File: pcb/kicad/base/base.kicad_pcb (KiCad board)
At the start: 2 copper layers, 94 parts, among them J1 CHIP_EN, J2 Vbatt_I-test, P1 J-Link SWD, P2 SMA, P3 Power Source, P4 CONN_01X08, U1 SAMB11G18A-edit, U2 XBee-PRO_900HP, Y1 32.768kHz, Y2 26MHz

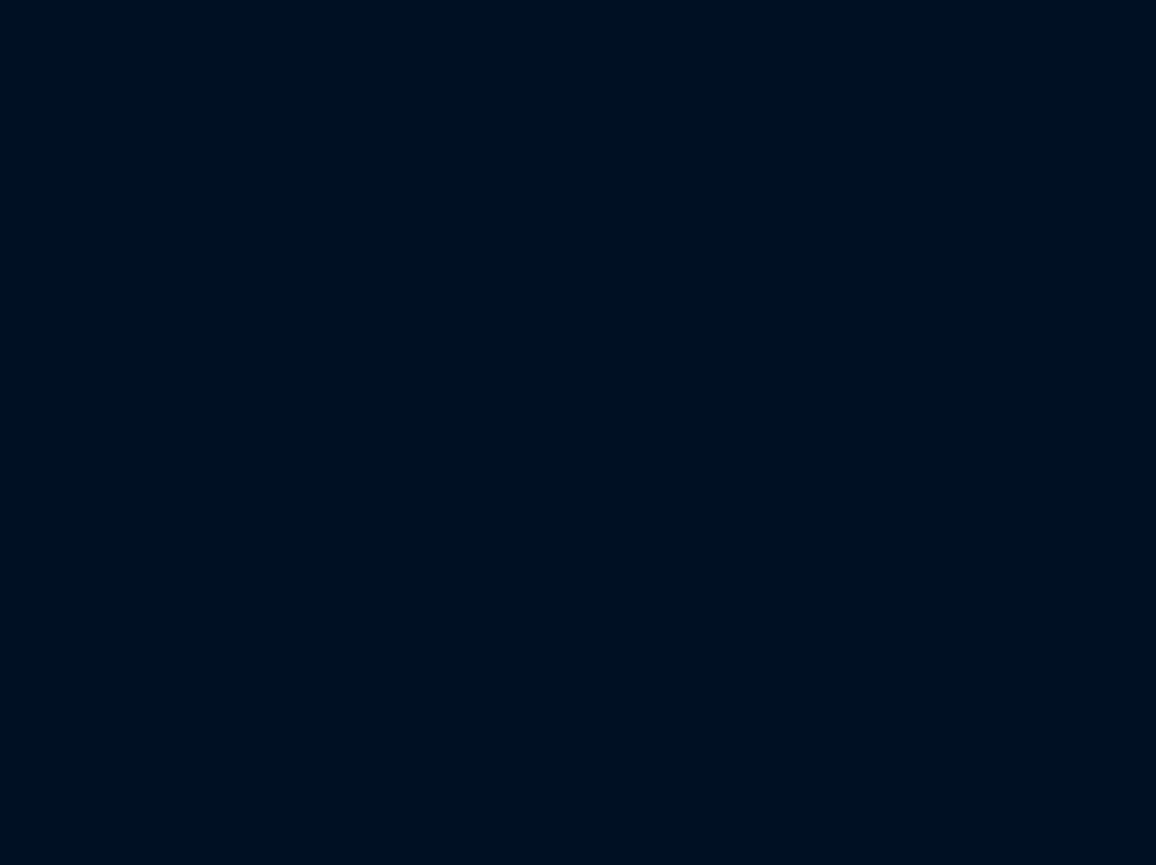
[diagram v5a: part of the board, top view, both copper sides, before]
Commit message: Add 16x4 LCD display symbol
Symbol and schematic started for the Crystalfontz display to be used
for user interface. Display contrast and LCD brightness settings need
to configured based on breadboard testing. Layout will be reworked to
properly accompany the mass pin usage of the display.
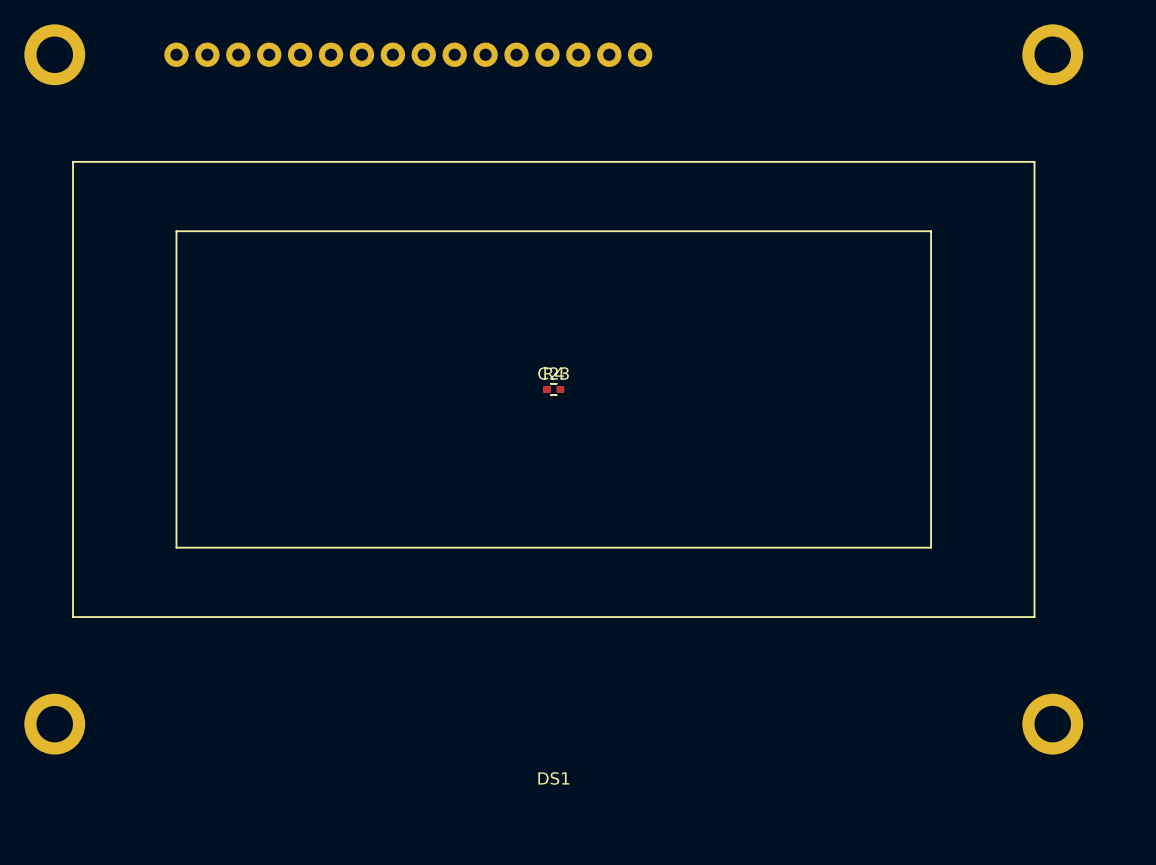
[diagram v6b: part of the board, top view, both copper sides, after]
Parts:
- added C23: C_Small, Capacitors_SMD:C_0402, F.Cu at (0.00, 0.00)
- added DS1: LCD16X4, CFAH1604A, F.Cu at (0.00, 0.00)
- added R4: 100, Capacitors_SMD:C_0402, F.Cu at (0.00, 0.00)
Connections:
- U1 pad 10: Net-(U1-Pad10) -> /DISP_B4
- U1 pad 11: Net-(U1-Pad11) -> /DISP_B3
- U1 pad 12: Net-(U1-Pad12) -> /DISP_B2
- U1 pad 13: /LP_GPIO_6 -> /DISP_B1
- U1 pad 14: /LP_GPIO_7 -> /DISP_B0
- U1 pad 15: /LP_GPIO_8 -> /DISP_E
- U1 pad 16: /LP_GPIO_9 -> /DISP_RW
- U1 pad 17: /LP_GPIO_10 -> /DISP_REG
- U1 pad 18: /LP_GPIO_11 -> Net-(U1-Pad18)
- U1 pad 19: /LP_GPIO_12 -> Net-(U1-Pad19)
- U1 pad 20: /LP_GPIO_13 -> Net-(U1-Pad20)
- U1 pad 7: Net-(U1-Pad7) -> /DISP_B7
- U1 pad 8: Net-(U1-Pad8) -> /DISP_B6
- U1 pad 9: Net-(U1-Pad9) -> /DISP_B5
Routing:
- net /LP_GPIO_6: track 33.6 -> 29.5 mm
- net /DISP_B1: track 0.00 -> 4.13 mm
- net /DISP_B0: track 0.00 -> 3.96 mm
- net /LP_GPIO_7: track 35.7 -> 31.7 mm
- net /LP_GPIO_8: track 37.7 -> 33.9 mm
- net /DISP_E: track 0.00 -> 3.79 mm
- net /LP_GPIO_9: track 39.8 -> 36.1 mm
- net /DISP_RW: track 0.00 -> 3.62 mm
- net /LP_GPIO_10: track 41.8 -> 38.3 mm
- net /DISP_REG: track 0.00 -> 3.45 mm
- net Net-(U1-Pad18): track 0.00 -> 3.28 mm
- net /LP_GPIO_11: track 43.8 -> 40.6 mm
- net Net-(U1-Pad19): track 0.00 -> 3.11 mm
- net /LP_GPIO_12: track 45.9 -> 42.8 mm
- net Net-(U1-Pad20): track 0.00 -> 2.93 mm
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
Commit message: Cleanup previous revision traces for new layout
Moving forward with full base station layout. Crystals, power caps, and
2.4GHz antenna placed. Mounting hole placements should coincide with
display mounting holes. May want to rotate XBee placement to allow push
buttons to be placed to the right of the display.
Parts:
- removed J1: CHIP_EN, Misc:Socket_Strip_Straight_1x02_Pitch2.54mm_Drill0.64mm
- removed P4: CONN_01X08, Misc:Socket_Strip_Straight_1x08_Pitch2.54mm_Drill0.64mm
- removed REF** (x9): Via_Stitch_Dia1.00mm_Drill0.64mm, Misc:Via_Stitch_Dia1.00mm_Drill0.64mm
- removed REF** (x45): Via_Stitch_Dia0.356mm_Drill0.254mm, Misc:Via_Stitch_Dia0.356mm_Drill0.254mm
- added AE1: 2.4-2.4835GHz, Antennas:Patch_Antenna_2.4GHz, F.Cu at (114.6, 82.7)
- C10: moved to B.Cu
- C13: moved to F.Cu
- Y1: footprint Crystals:Crystal_C38-LF_d3.0mm_l8.0mm_Horizontal_1EP_style1 -> Crystals:Crystal_SMD_3215-2pin_3.2x1.5mm
- moved DS1 194.3 mm to (139.3, 135.4), turned to 180 degrees
- moved P2 144.1 mm to (-11.2, 79.8)
- moved C19 60.1 mm to (185.0, 133.1)
- moved R2 60.1 mm to (201.7, 133.1)
- moved R3 60.1 mm to (191.5, 133.1)
- moved P1 60.1 mm to (184.5, 135.2)
- moved R1 8.08 mm to (135.4, 83.6)
- moved FB1 4.63 mm to (138.8, 81.8)
- moved C13 2.86 mm to (142.8, 85.3)
- moved C10 2.21 mm to (144.4, 87.4)
- moved Y1 1.54 mm to (154.1, 88.9), turned to 270 degrees
- moved C9 1.44 mm to (145.7, 85.5)
- moved Y2 1.39 mm to (146.4, 82.3)
- moved C8 1.34 mm to (147.0, 79.1)
- moved C18 0.69 mm to (151.9, 89.6)
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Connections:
- P2 pad 1: /SIG_2.4G -> Net-(P2-Pad1)
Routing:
- net Net-(C14-Pad1): track 238.7 -> 2.69 mm, vias 6 -> 1
- net /+3.3V: track 273.4 -> 95.4 mm, vias 9 -> 3
- net /UART_CTS: track 67.0 -> 0.34 mm, vias 1 -> 0
- net /UART_RX: track 65.1 -> 0.00 mm, vias 1 -> 0
- net /UART_TX: track 64.2 -> 0.00 mm, vias 1 -> 0
- net /UART_RTS: track 58.7 -> 0.00 mm, vias 1 -> 0
- net /LP_GPIO_13: track 45.0 -> 0.00 mm, vias 1 -> 0
- net /LP_GPIO_12: track 42.8 -> 0.00 mm, vias 1 -> 0
- net /LP_GPIO_11: track 40.6 -> 0.00 mm, vias 1 -> 0
- net /LP_GPIO_10: track 38.3 -> 0.00 mm, vias 1 -> 0
- net Net-(P1-Pad15): track 37.8 -> 0.00 mm, vias 3 -> 0
- net /LP_GPIO_9: track 36.1 -> 0.00 mm, vias 1 -> 0
- net /LP_GPIO_8: track 33.9 -> 0.00 mm, vias 1 -> 0
- net /LP_GPIO_7: track 31.7 -> 0.00 mm, vias 1 -> 0
- net /SWDIO: track 30.6 -> 0.00 mm, vias 1 -> 0
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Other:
- net class Default: via_dia 0.3302 -> 0.3556
- net class Power added: clearance 0.127, trace_width 0.762, via_dia 0.508, via_drill 0.381
- board text added: "0.2"
- board text added: "March 30, 2017"
- board text removed: "0.1"
- board text removed: "March 5, 2017"

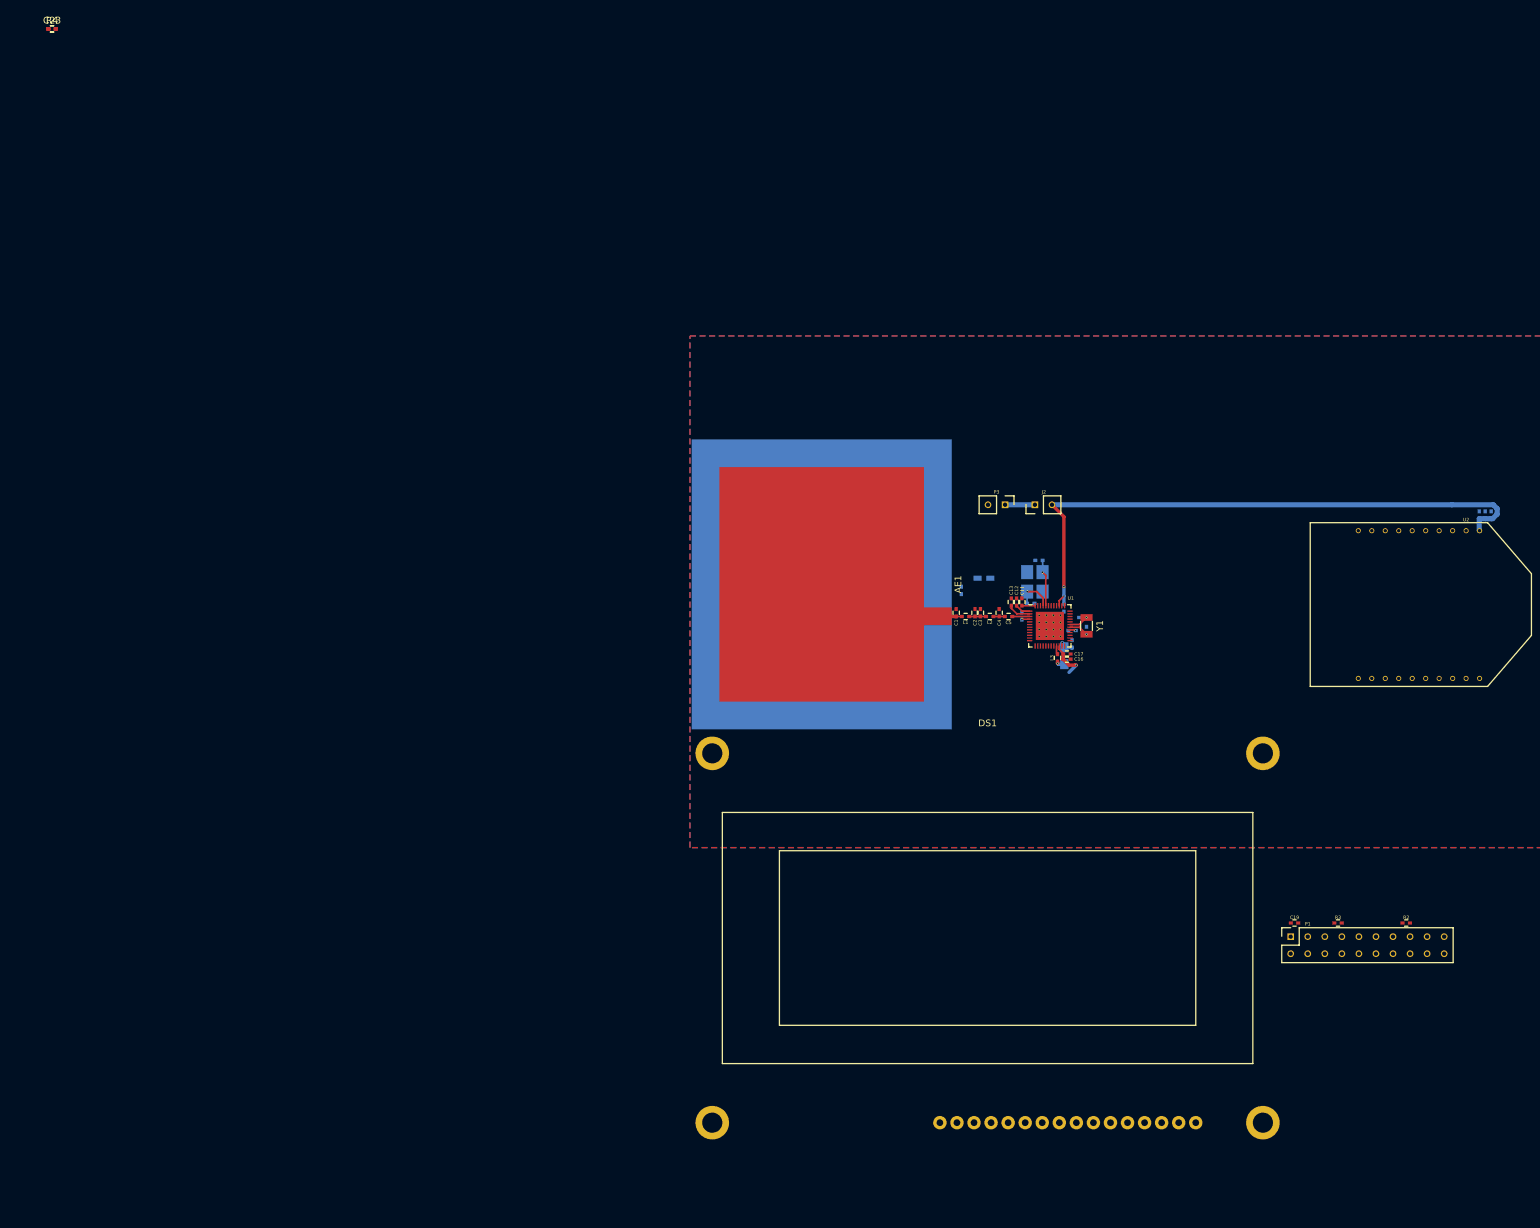
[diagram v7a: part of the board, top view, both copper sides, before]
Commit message: Add initial display connections
Traces can be carefully placed underneath display footprint due to
elevated model. Patch antenna copper voids need to be understood.
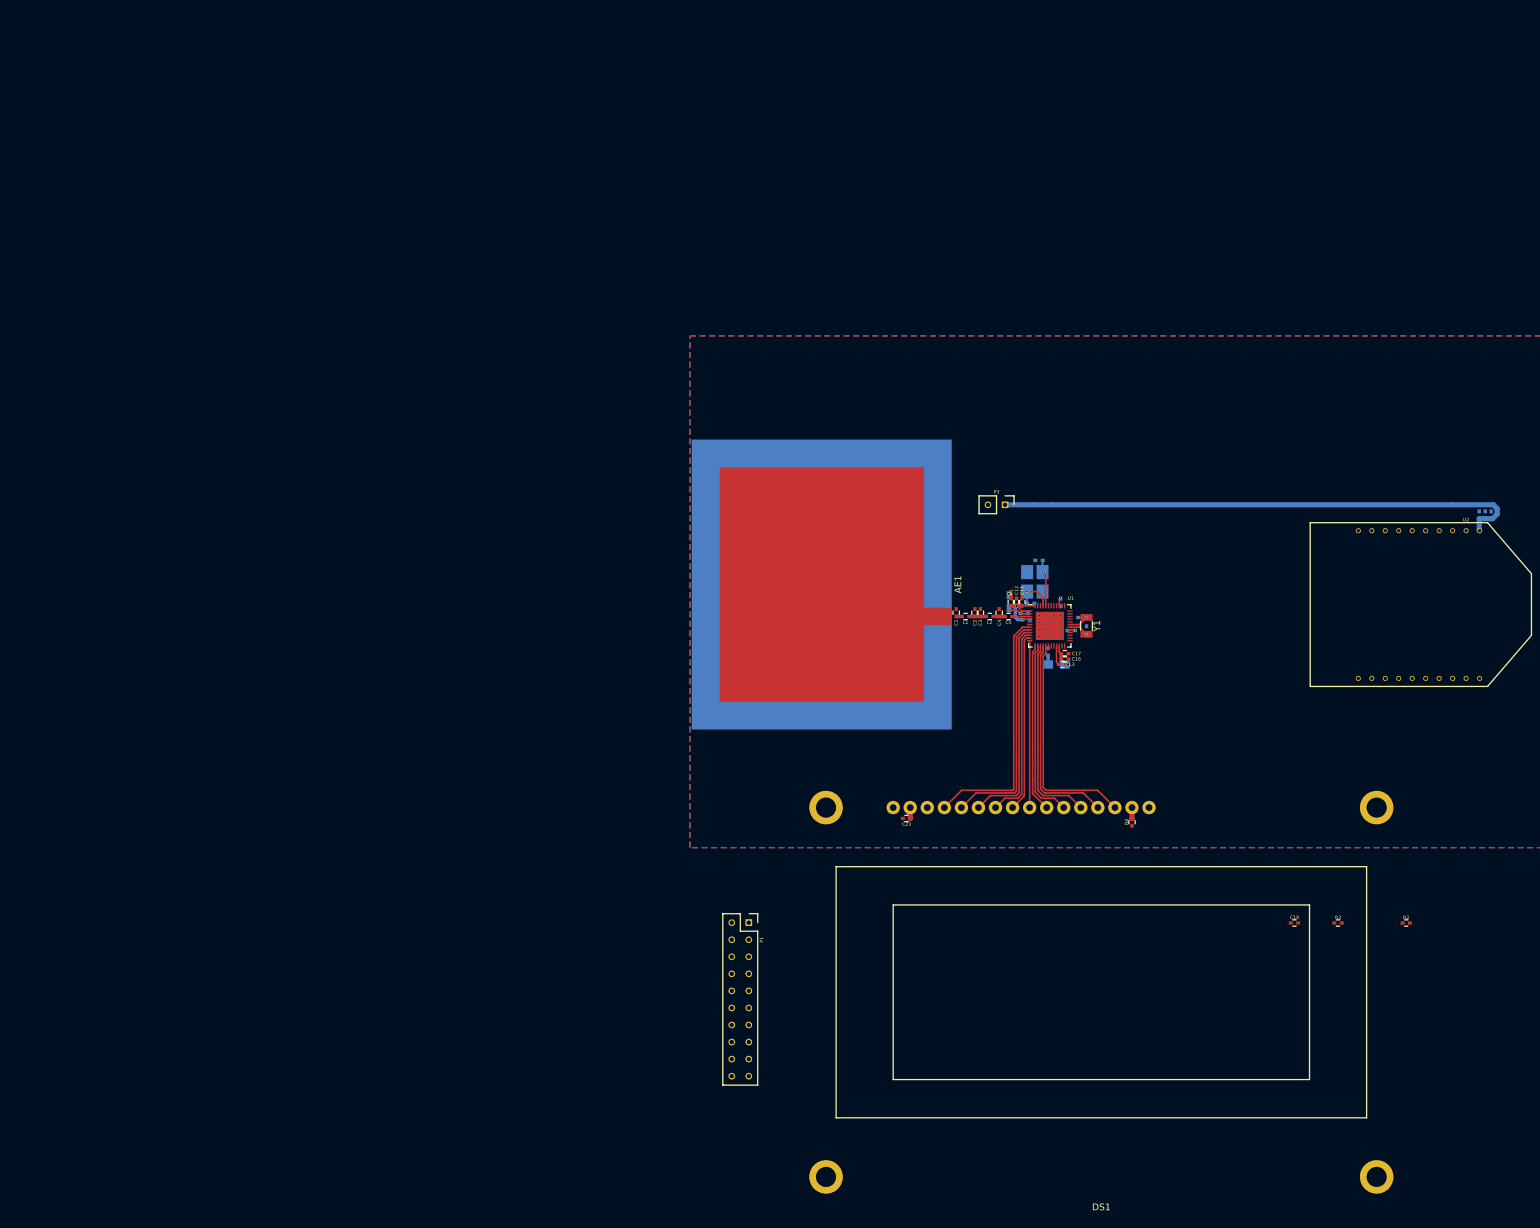
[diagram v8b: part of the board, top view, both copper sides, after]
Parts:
- removed J2: Vbatt_I-test, Misc:Socket_Strip_Straight_1x02_Pitch2.54mm_Drill0.64mm
- C13: moved to B.Cu
- R1: moved to F.Cu
- moved R4 199.5 mm to (160.8, 118.1), turned to 90 degrees
- moved C23 173.3 mm to (127.3, 117.6)
- moved P1 80.7 mm to (103.8, 133.1), turned to 0 degrees
- moved DS1 18.8 mm to (156.3, 143.5), turned to 0 degrees
- moved R1 7.64 mm to (142.8, 85.3)
- moved FB1 5.13 mm to (142.5, 85.3), turned to 270 degrees
- moved C14 3.75 mm to (148.3, 92.8)
- moved C13 2.58 mm to (144.8, 87.0), turned to 0 degrees
- moved L4 1.74 mm to (149.6, 94.6), turned to 180 degrees
- moved L3 1.22 mm to (150.5, 94.6), turned to 0 degrees
- moved C15 0.96 mm to (150.2, 85.4)
- moved C10 0.85 mm to (145.1, 88.0), turned to 0 degrees
- moved C17 0.31 mm to (150.8, 93.0)
- moved C16 0.31 mm to (150.8, 93.8)
- moved C18 0.13 mm to (151.8, 89.6)
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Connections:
- P3 pad 1: Net-(J2-Pad1) -> /+3.3V
- U1 pad 10: /DISP_B4 -> /DISP_B0
- U1 pad 11: /DISP_B3 -> /DISP_B1
- U1 pad 13: /DISP_B1 -> /DISP_B3
- U1 pad 14: /DISP_B0 -> /DISP_B4
- U1 pad 15: /DISP_E -> /DISP_B5
- U1 pad 16: /DISP_RW -> /DISP_B6
- U1 pad 17: /DISP_REG -> /DISP_B7
- U1 pad 7: /DISP_B7 -> /DISP_REG
- U1 pad 8: /DISP_B6 -> /DISP_RW
- U1 pad 9: /DISP_B5 -> /DISP_E
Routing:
- net /DISP_REG: track 0.00 -> 37.2 mm
- net /DISP_RW: track 0.00 -> 34.6 mm
- net /DISP_B7: track 0.00 -> 33.1 mm
- net /DISP_E: track 0.00 -> 31.9 mm
- net /DISP_B6: track 0.00 -> 31.1 mm
- net /DISP_B0: track 0.00 -> 29.3 mm
- net /DISP_B5: track 0.00 -> 29.1 mm
- net /DISP_B4: track 0.00 -> 27.1 mm
- net /DISP_B1: track 0.00 -> 26.6 mm
- net /DISP_B3: track 0.00 -> 25.1 mm
- net /DISP_B2: track 0.00 -> 24.9 mm
- net /+3.3V: track 95.4 -> 82.4 mm, vias 3 -> 1
- net Net-(C10-Pad1): track 5.44 -> 10.0 mm, vias 1 -> 2
- net Net-(J2-Pad1): track 4.44 -> 0.00 mm
- net /SIG_2.4G: track 3.58 -> 0.85 mm
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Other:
- net class Default: via_dia 0.3556 -> 0.381
